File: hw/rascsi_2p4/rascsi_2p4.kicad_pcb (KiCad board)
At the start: 2 copper layers, 65 x 56 mm, 72 parts, among them J1 Raspberry_Pi_2_3, J10 Conn_01x04_Male, J2 DNP, J20 171826-4, J3 Conn_02x25_Odd_Even, J4 I2C Pinout, J5 DNP, J6 CONNFLY DB-25, J7 DNP, J8 USB_B_Micro, J9 Conn_02x25_Odd_Even, U1 SN74LS641-1DW, U2 SN74LS641-1DW, U3 SN74LS641-1DW, U4 SN74LS641-1DW, U5 UCC5606PWPTR, U6 UCC5606PWPTR, X1 Mac, X3 Mac, X7 Pi, X8 Pi

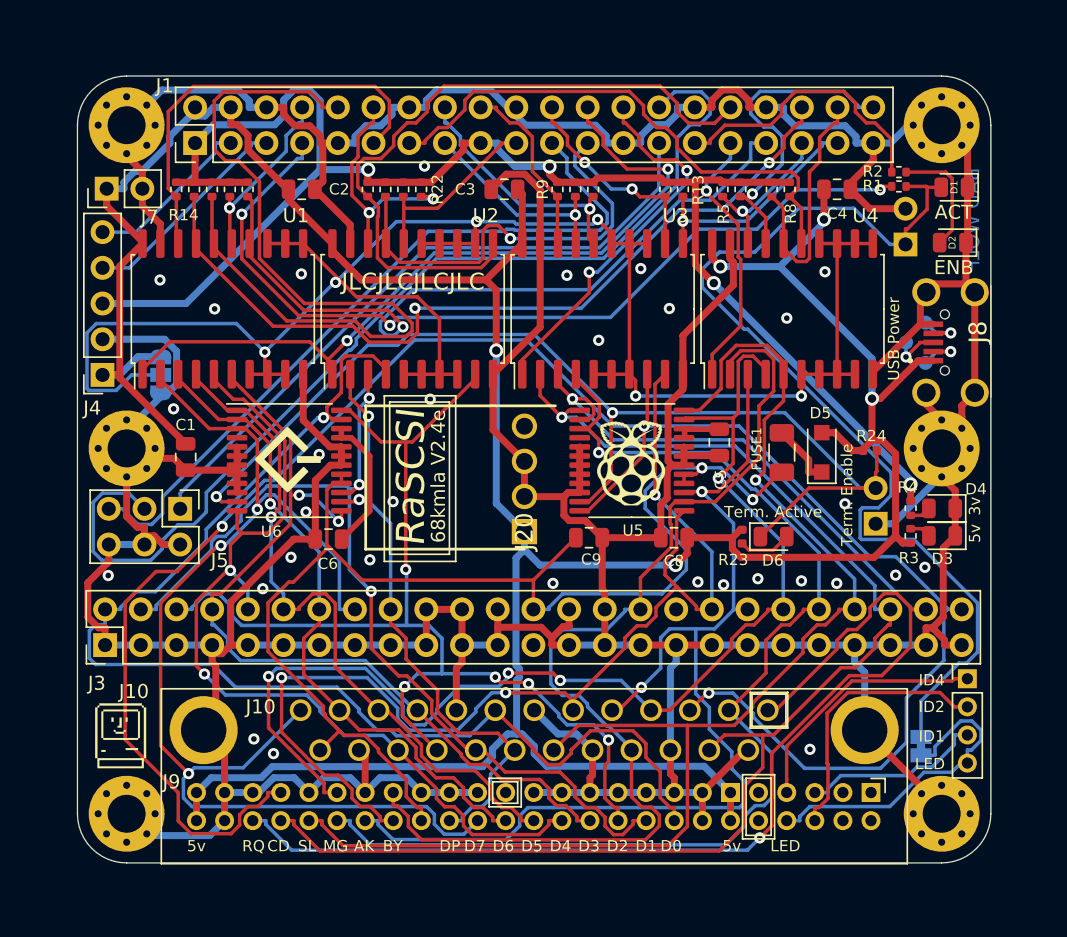
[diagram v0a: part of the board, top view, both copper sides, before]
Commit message: swapped R18 and R22 slightly moved R14 to R18
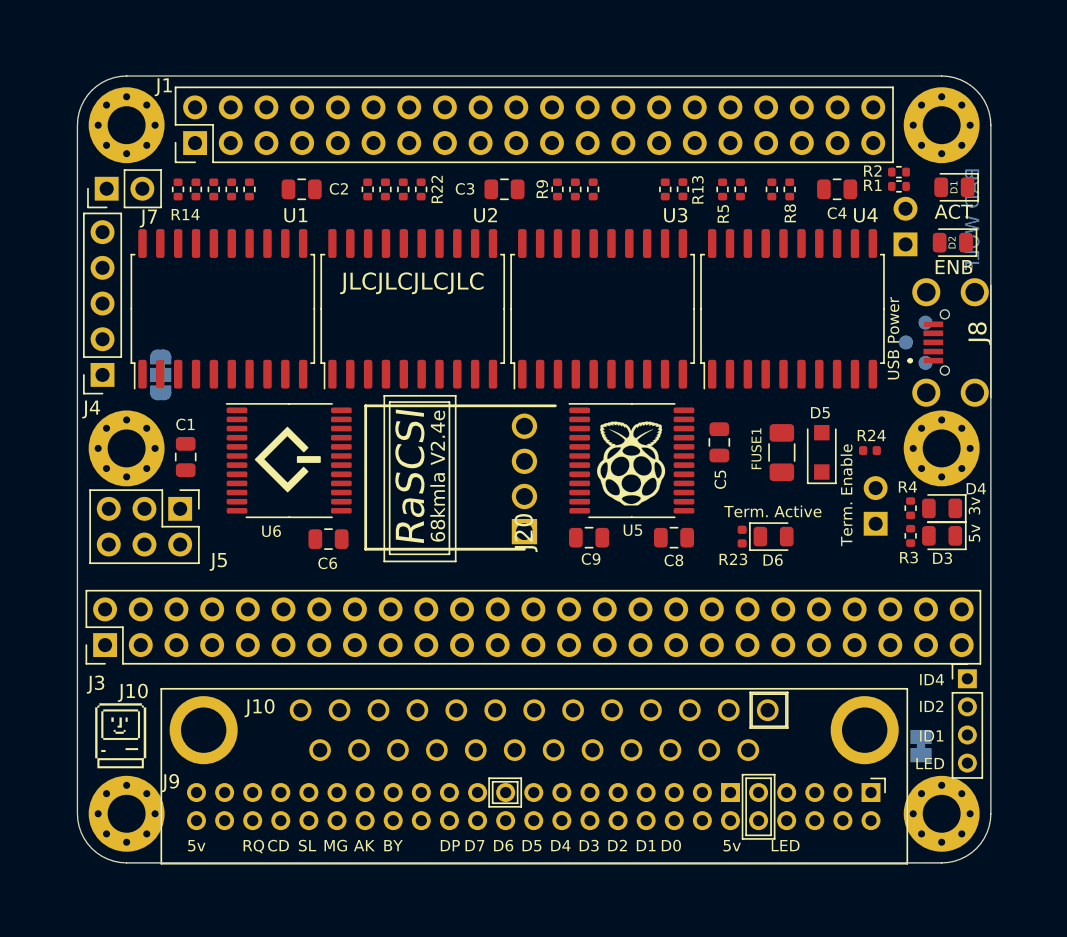
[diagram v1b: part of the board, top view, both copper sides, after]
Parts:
- moved R14 0.13 mm to (181.7, 50.6)
- moved R15 0.13 mm to (182.9, 50.6)
- moved R17 0.13 mm to (185.5, 50.6)
- moved R18 0.13 mm to (186.7, 50.6)
- moved R16 0.13 mm to (184.2, 50.6)
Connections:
- R19 pad 2: PI-D2 -> PI-DP
- R22 pad 2: PI-DP -> PI-D2
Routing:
- net GND: track 542.9 -> 0.00 mm, vias 31 -> 0
- net +5V: track 231.1 -> 0.00 mm, vias 5 -> 0
- net C-I_O: track 143.8 -> 0.00 mm, vias 3 -> 0
- net PULLUP_OC: track 131.8 -> 0.00 mm, vias 6 -> 0
- net C-REQ: track 112.6 -> 0.00 mm, vias 2 -> 0
- net +3V3: track 110.7 -> 0.00 mm, vias 4 -> 0
- net C-C_D: track 95.1 -> 0.00 mm, vias 1 -> 0
- net C-SEL: track 94.0 -> 0.00 mm, vias 1 -> 0
- net TERMPOW: track 90.1 -> 0.00 mm, vias 2 -> 0
- net C-D0: track 88.4 -> 0.00 mm, vias 1 -> 0
- net C-D7: track 84.3 -> 0.00 mm, vias 3 -> 0
- net C-RST: track 82.7 -> 0.00 mm, vias 4 -> 0
- net C-MSG: track 82.1 -> 0.00 mm, vias 1 -> 0
- net C-BSY: track 79.7 -> 0.00 mm, vias 3 -> 0
- net C-D2: track 78.3 -> 0.00 mm, vias 5 -> 0
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
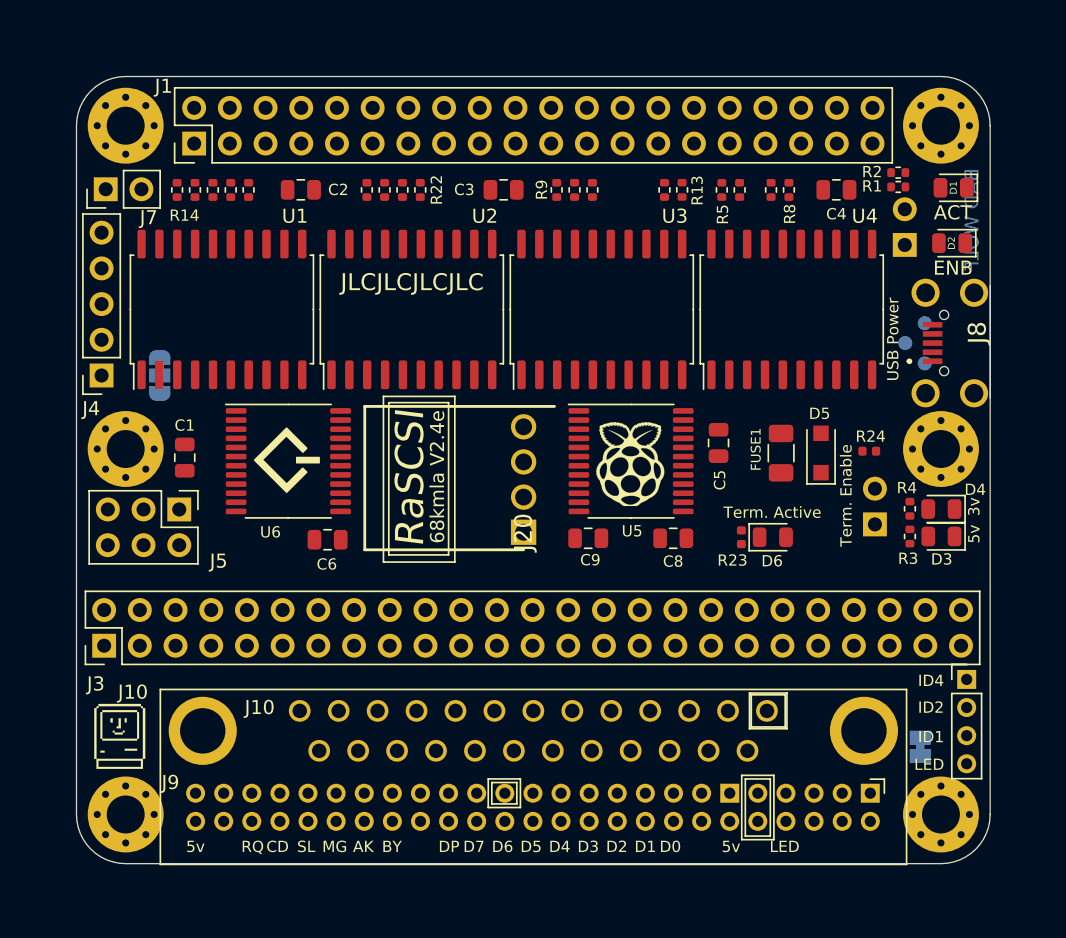
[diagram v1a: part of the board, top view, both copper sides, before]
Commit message: newly routed with 71 vias
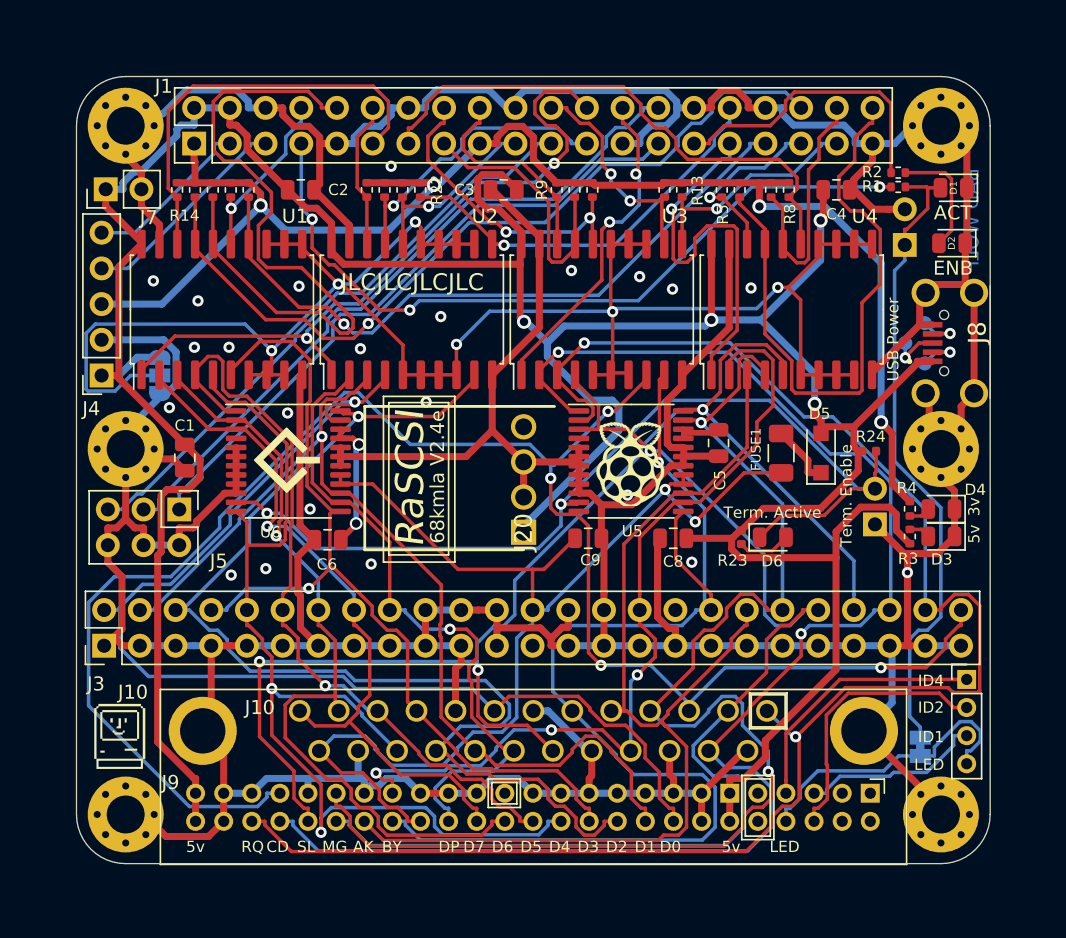
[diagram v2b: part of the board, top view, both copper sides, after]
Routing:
- net GND: track 0.00 -> 552.9 mm, vias 0 -> 22
- net +5V: track 0.00 -> 246.0 mm, vias 0 -> 4
- net PULLUP_OC: track 0.00 -> 126.6 mm, vias 0 -> 6
- net C-I_O: track 0.00 -> 123.6 mm, vias 0 -> 4
- net C-REQ: track 0.00 -> 119.5 mm, vias 0 -> 2
- net C-C_D: track 0.00 -> 106.0 mm, vias 0 -> 2
- net +3V3: track 0.00 -> 103.2 mm, vias 0 -> 4
- net C-SEL: track 0.00 -> 95.2 mm, vias 0 -> 3
- net C-RST: track 0.00 -> 91.5 mm, vias 0 -> 2
- net TERMPOW: track 0.00 -> 84.6 mm, vias 0 -> 2
- net C-BSY: track 0.00 -> 83.9 mm, vias 0 -> 1
- net C-MSG: track 0.00 -> 83.4 mm, vias 0 -> 1
- net C-D0: track 0.00 -> 81.8 mm, vias 0 -> 1
- net C-D2: track 0.00 -> 81.1 mm, vias 0 -> 1
- net C-ACK: track 0.00 -> 75.4 mm
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
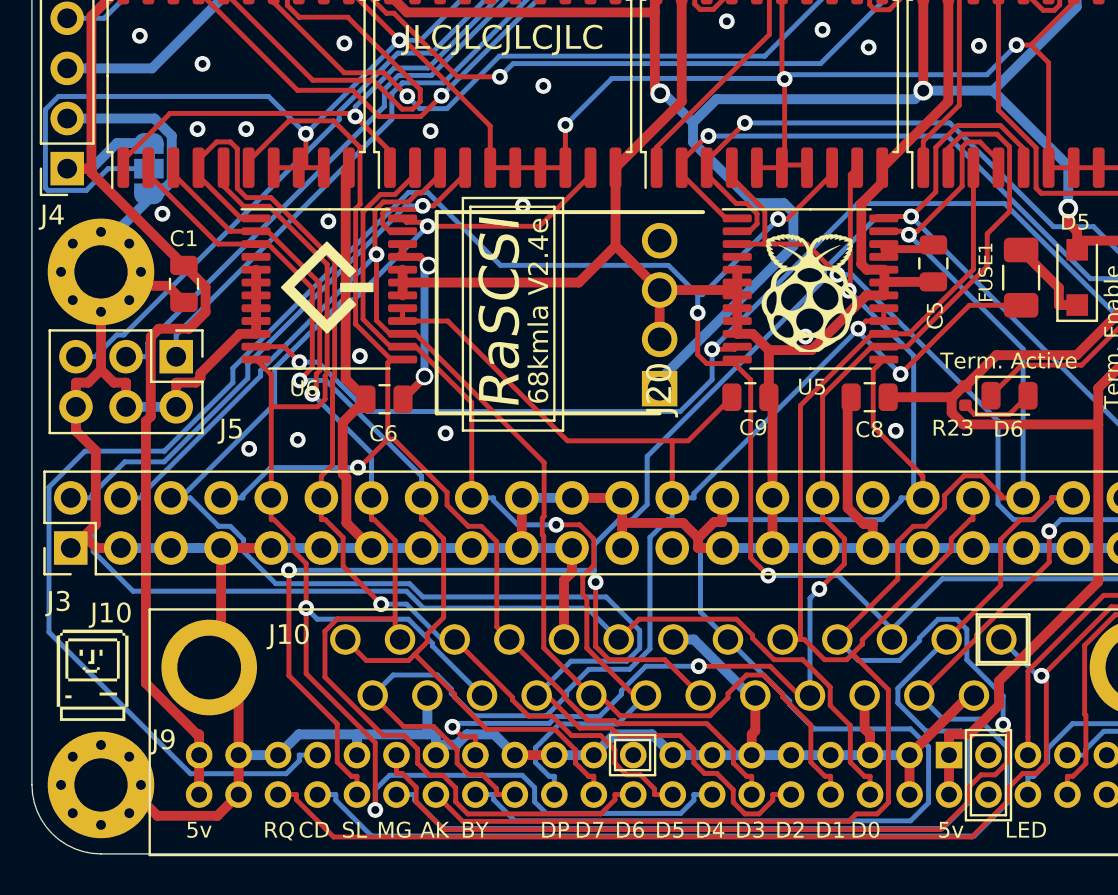
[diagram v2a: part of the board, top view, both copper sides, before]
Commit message: added more GND for cooling term ICs
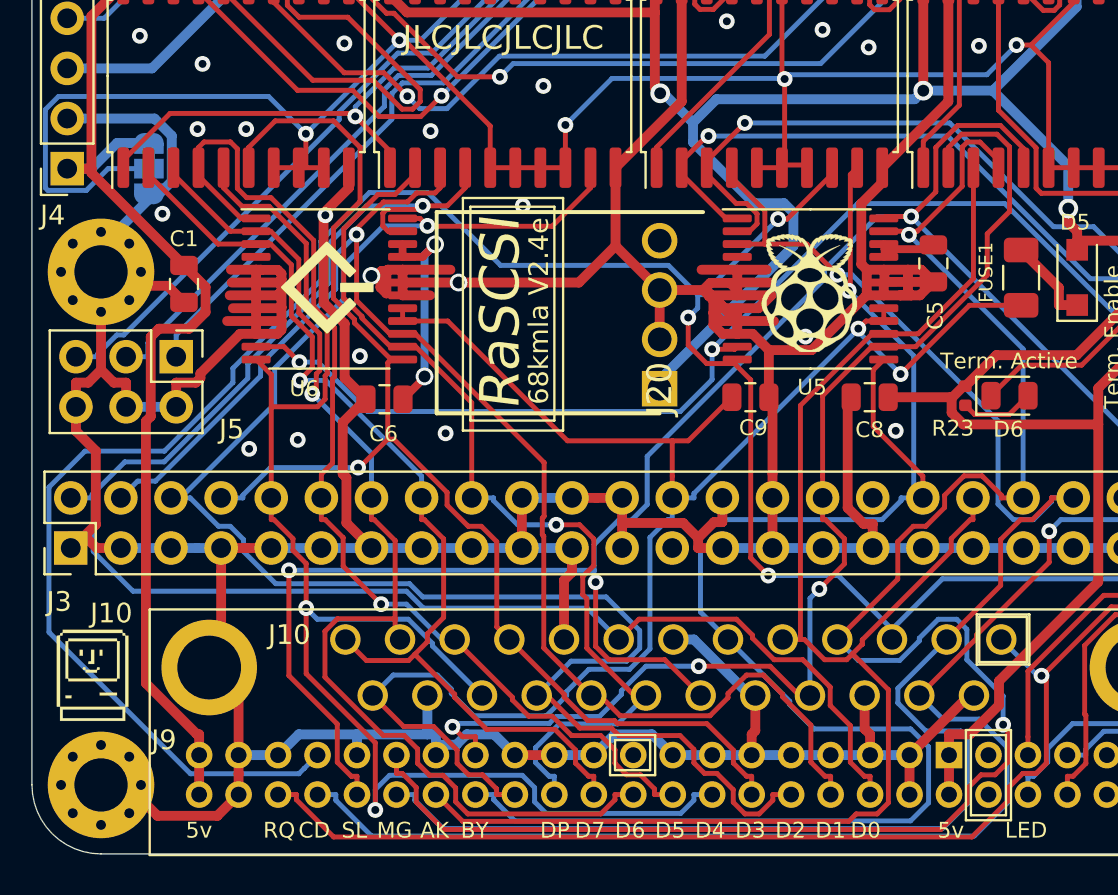
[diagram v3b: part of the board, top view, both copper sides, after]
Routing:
- net GND: track 552.9 -> 609.4 mm, vias 22 -> 24
- net C-D1: track 70.5 -> 72.1 mm
- net C-D0: track 81.8 -> 83.5 mm
- net POWER_REG_U4: track 9.46 -> 11.1 mm
- net C-I_O: track 123.6 -> 125.0 mm
- net C-D2: track 81.1 -> 82.5 mm
- net C-D3: track 63.2 -> 64.6 mm
- net C-DP: track 47.9 -> 48.8 mm

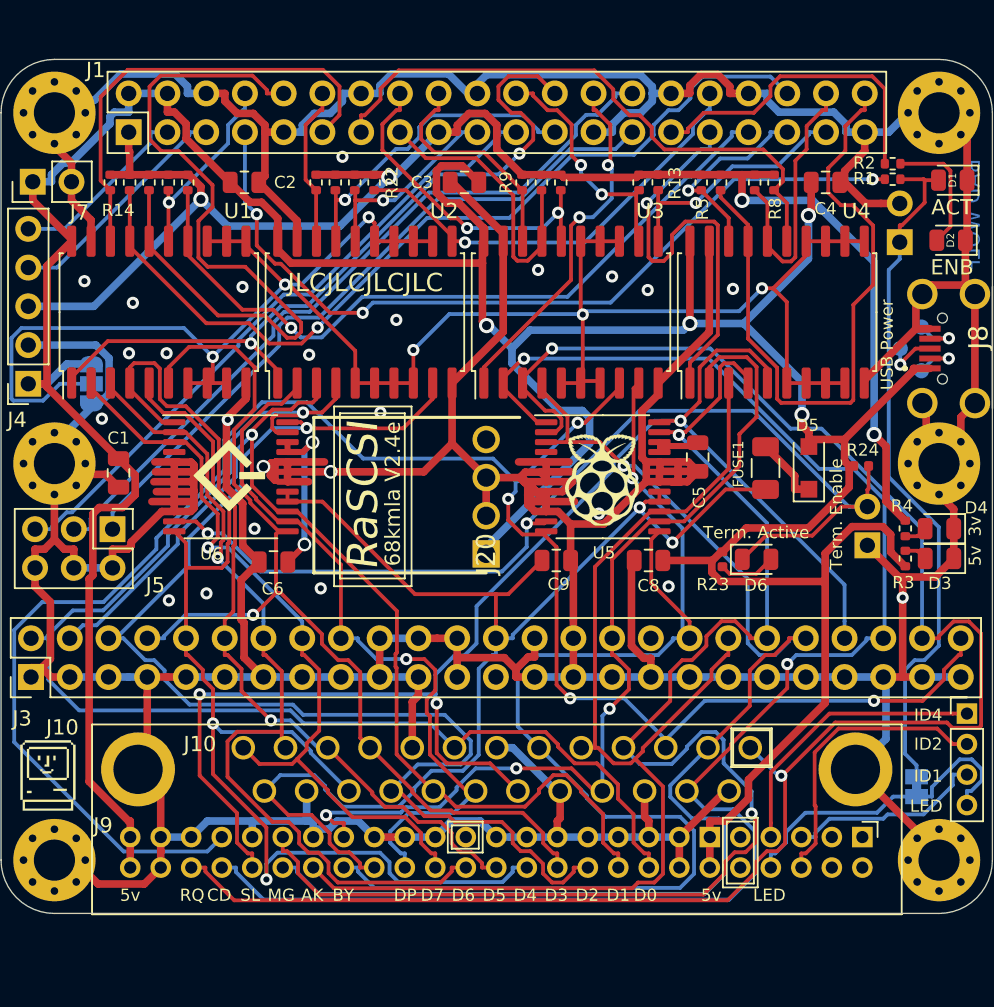
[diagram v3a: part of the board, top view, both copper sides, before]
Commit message: made 25pin and USB conn placeable by JLCPCB
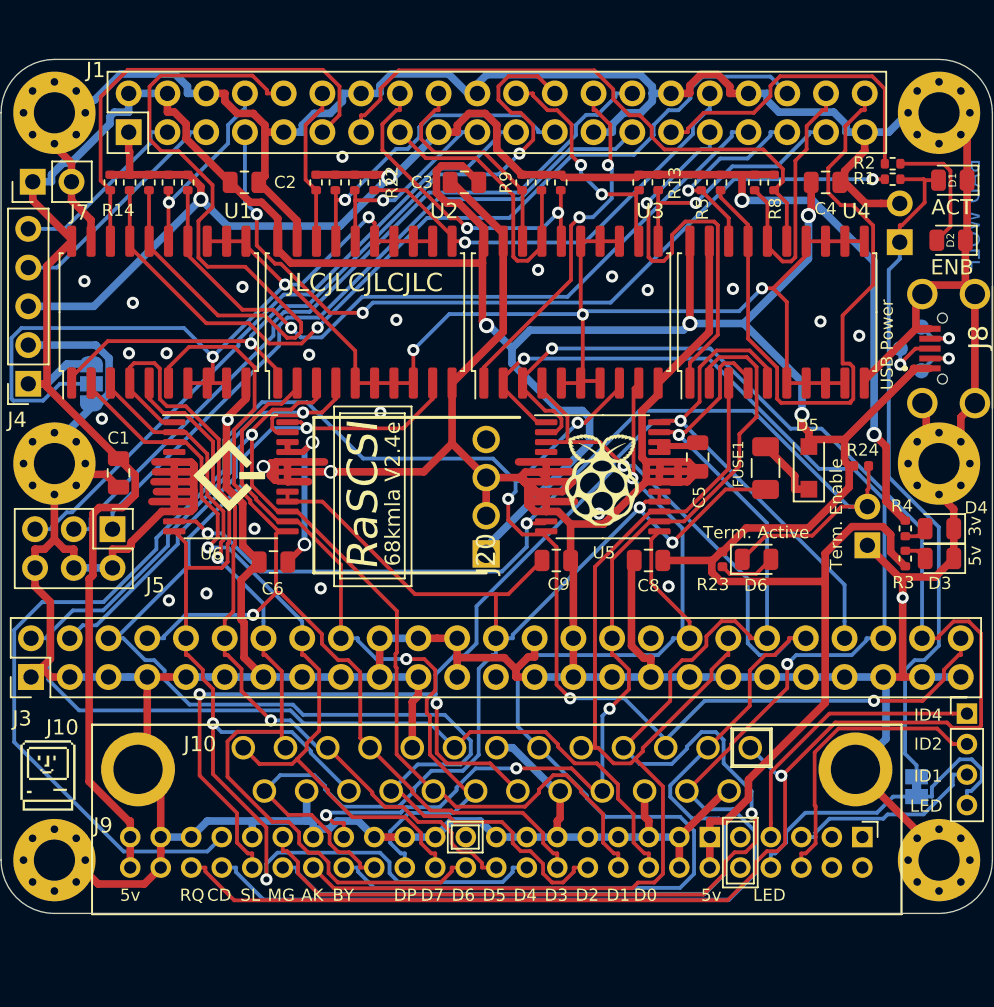
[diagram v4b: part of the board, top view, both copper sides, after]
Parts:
- J3: footprint Connector_PinHeader_2.54mm:PinHeader_2x25_P2.54mm_Vertical -> amiga:PinHeader_2x25_P2.54mm_Vertical_JLCPCB_hand_mount
- J6: footprint SamacSys_Parts:L717SDB25PA4CH4F -> SamacSys_Parts:L717SDB25PA4CH4F_JLCPCB_hand_mount; moved to F.Cu
- J8: footprint SamacSys_Parts:U254051N4BH806 -> SamacSys_Parts:U254051N4BH806_JLCPCB_hand_mount
- moved J6 33.2 mm to (190.4, 87.6), turned to 0 degrees
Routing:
- net PI-ACK: track 43.8 -> 44.7 mm
- net GND: vias 24 -> 26

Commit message: fixed logo position changed origin settings and gerber/pos export setting
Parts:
- J6: moved to B.Cu
- moved C1 174.6 mm to (12.2, 29.6)
- moved C2 174.6 mm to (20.5, 10.6)
- moved C3 174.6 mm to (34.9, 10.6)
- moved C4 174.6 mm to (58.6, 10.6)
- moved C5 174.6 mm to (50.2, 28.6)
- moved C6 174.6 mm to (22.4, 35.5)
- moved C8 174.6 mm to (47.0, 35.4)
- moved C9 174.6 mm to (40.9, 35.4)
- moved D1 174.6 mm to (66.9, 10.4)
- moved D2 174.6 mm to (66.8, 14.4)
- moved D3 174.6 mm to (66.0, 35.2)
- moved D4 174.6 mm to (66.0, 33.3)
- moved D5 174.6 mm to (57.5, 29.3)
- moved D6 174.6 mm to (54.0, 35.3)
- moved FUSE1 174.6 mm to (54.6, 29.3)
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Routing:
- net GND: track 609.4 -> 552.9 mm, vias 26 -> 0
- net C-D1: track 72.1 -> 70.5 mm
- net C-D0: track 83.5 -> 81.8 mm
- net POWER_REG_U4: track 11.1 -> 9.46 mm
- net C-I_O: track 125.0 -> 123.6 mm
- net C-D2: track 82.5 -> 81.1 mm
- net C-D3: track 64.6 -> 63.2 mm
- net PI-ACK: track 44.7 -> 43.8 mm
- net C-DP: track 48.8 -> 47.9 mm
- net +5V: track 246.0 -> 245.5 mm
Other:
- board text added: "68kmla V2.4et"
- board text removed: "68kmla V2.4e"
